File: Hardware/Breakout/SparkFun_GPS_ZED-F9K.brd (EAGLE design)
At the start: 43.2 x 43.2 mm, 104 parts, among them J1 QWIIC_RIGHT_ANGLE, J4 U.FL, J6 QWIIC_RIGHT_ANGLE, U2 3.3V, U3 UBLOX_ZED_F9K, U4 TRIPLE_BUFFER_74LVC3G07

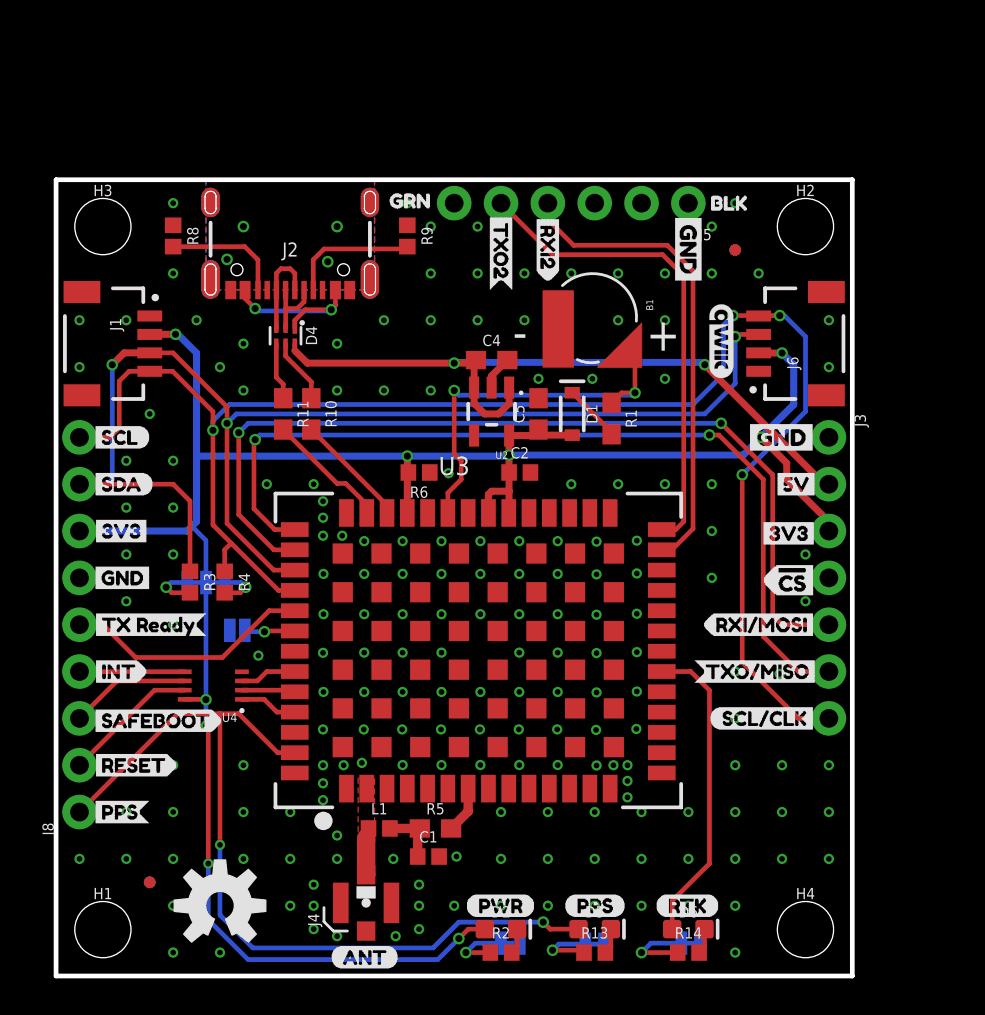
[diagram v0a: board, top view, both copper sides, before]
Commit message: Moves buzzard labels to their own folder - updates breakout board with better labeling
* fixes I2C lines being backwards
* Moves D+ and D- lines around
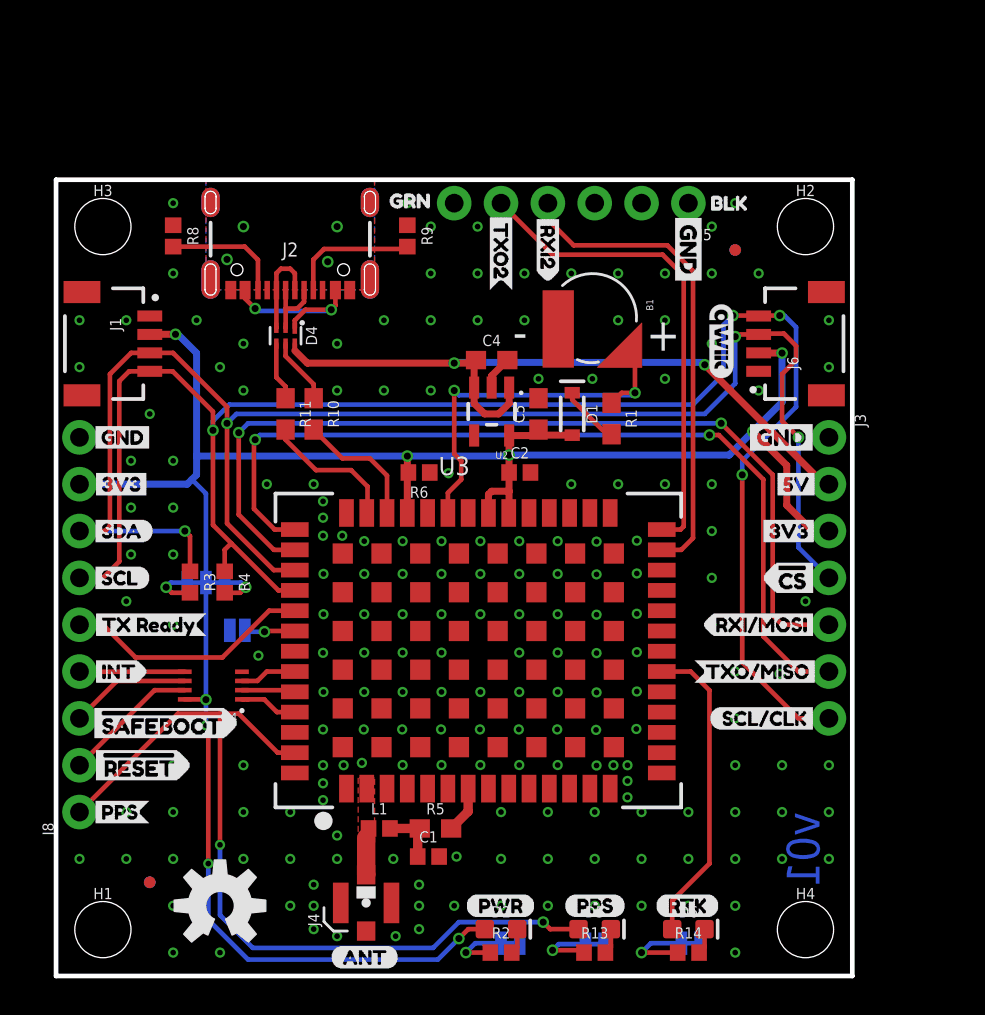
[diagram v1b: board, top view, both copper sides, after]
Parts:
- removed U$32: (no value), bottom labels:SAFEBOOT3
- added U$44: (no value), corrected_safe_reset:#RESET1
- U$10: device ALL labels:SAFEBOOT1 -> corrected_safe_reset:#SAFEBOOT0
- U$28: device bottom labels:RESET4 -> corrected_safe_reset:#SAFEBOOT3
- U$7: device ALL labels:RESET3 -> corrected_safe_reset:#RESET2
- moved U$11 7.62 mm to (1.78, 21.6)
- moved U$39 7.62 mm to (6.10, 21.6)
- moved U$41 7.62 mm to (6.48, 29.2)
- moved U$6 7.62 mm to (1.78, 29.2)
- moved U$7 5.71 mm to (7.49, 11.4), flipped to the bottom
- moved U$28 3.17 mm to (10.0, 14.0)
- moved U$40 2.54 mm to (6.35, 26.7)
- moved U$12 2.54 mm to (1.78, 24.1)
- moved U$3 2.54 mm to (1.78, 26.7)
- moved U$42 2.54 mm to (6.35, 24.1)
- moved U$10 0.40 mm to (1.40, 13.7)
- moved R10 0.13 mm to (14.0, 30.5)
- moved U$47 0.13 mm to (30.9, 3.56)
- moved R11 0.13 mm to (12.4, 30.5)
- moved U$19 0.13 mm to (38.0, 24.1)
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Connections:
- removed net !CS: J3.4
- net 3.3V: now also J8.8; no longer J8.7
- net GND: now also J8.9; no longer J8.6
- net SCL/CLK: now also J8.6; no longer J8.9
- net SDA/!CS: now also J3.4, J8.7; no longer J8.8
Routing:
- net SDA/!CS: track 69.4 -> 85.7 mm, vias 3 -> 4
- net SCL/CLK: track 86.9 -> 93.9 mm
- net DMINUS: track 6.22 -> 7.04 mm
- net DPLUS: track 6.71 -> 7.49 mm
- net GND: vias 188 -> 189
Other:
- board text added: "v01"

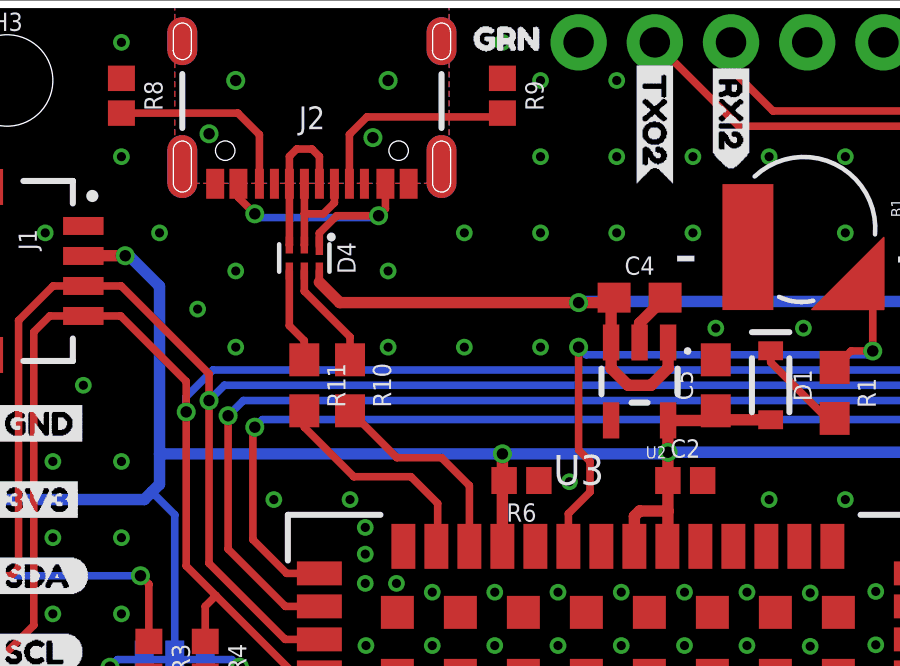
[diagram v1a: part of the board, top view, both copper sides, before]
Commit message: Fixes routing for ESD protection IC
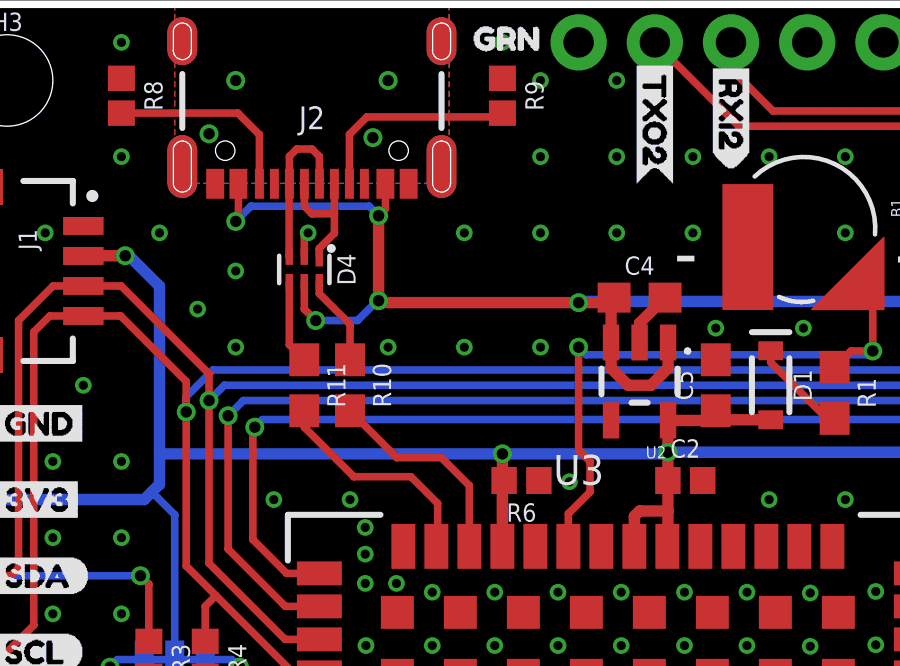
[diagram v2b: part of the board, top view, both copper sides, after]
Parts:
- moved D4 0.38 mm to (12.4, 34.3)
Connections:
- removed net N$16: D4.5, R10.1
- removed net V_USB: D4.1, J2.VBUS1, J2.VBUS2
- new net N$9: D4.6, R10.1
- net GND: now also D4.2
- net N$7: now also D4.1; no longer D4.2
- net VIN: now also D4.5, J2.VBUS1, J2.VBUS2; no longer D4.6
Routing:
- net VIN: track 39.1 -> 50.7 mm, vias 2 -> 6
- net V_USB: track 9.23 -> 0.00 mm, vias 2 -> 0
- net N$16: track 3.59 -> 0.00 mm
- net N$9: track 0.00 -> 3.00 mm
- net GND: track 1.85 -> 2.69 mm
- net N$7: track 3.83 -> 4.51 mm
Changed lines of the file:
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@@
 <attribute name="VALUE" x="26.924" y="30.48" size="0.6096" layer="27" font="vector" ratio="20" rot="R90" align="top-center"/>
 </element>
-<element name="D4" library="SparkFun-IC-Power" package="SOT886" value="PRTR5V0U2F" x="12.446" y="34.7218" smashed="yes" rot="R270">
-<attribute name="NAME" x="13.546" y="34.7218" size="0.6096" layer="25" ratio="20" rot="R270" align="bottom-center"/>
-<attribute name="PROD_ID" value="DIO-14084" x="12.446" y="34.7218" size="1.778" layer="27" font="vector" ratio="15" rot="R270" display="off"/>
-<attribute name="VALUE" x="11.546" y="34.7218" size="0.6096" layer="27" ratio="20" rot="R270" align="top-center"/>
+<element name="D4" library="SparkFun-IC-Power" package="SOT886" value="PRTR5V0U2F" x="12.446" y="34.3408" smashed="yes" rot="R270">
+<attribute name="NAME" x="13.546" y="34.3408" size="0.6096" layer="25" ratio="20" rot="R270" align="bottom-center"/>
+<attribute name="PROD_ID" value="DIO-14084" x="12.446" y="34.3408" size="1.778" layer="27" font="vector" ratio="15" rot="R270" display="off"/>
+<attribute name="VALUE" x="11.546" y="34.3408" size="0.6096" layer="27" ratio="20" rot="R270" align="top-center"/>
 </element>
 <element name="R10" library="SparkFun-Resistors" package="0603" value="27" x="13.97" y="30.48" smashed="yes" rot="R270">
@@
 <via x="17.78" y="31.75" extent="1-16" drill="0.3048"/>
 <via x="15.24" y="31.75" extent="1-16" drill="0.3048"/>
-<via x="15.24" y="34.29" extent="1-16" drill="0.3048"/>
 <via x="14.478" y="10.45" extent="1-16" drill="0.3048"/>
 <via x="14.478" y="9.5356" extent="1-16" drill="0.3048"/>
@@
 <via x="38.1" y="31.75" extent="1-16" drill="0.3048"/>
 <via x="35.56" y="34.29" extent="1-16" drill="0.3048"/>
+<contactref element="D4" pad="2"/>
+<via x="12.573" y="35.56" extent="1-16" drill="0.3048"/>
+<wire x1="12.446" y1="34.7708" x2="12.446" y2="35.433" width="0.254" layer="1"/>
+<wire x1="12.446" y1="35.433" x2="12.573" y2="35.56" width="0.254" layer="1"/>
 </signal>
 <signal name="3.3V">
@@
 <wire x1="8.114" y1="15" x2="8.128" y2="14.986" width="0.254" layer="1"/>
 <via x="8.128" y="14.986" extent="1-16" drill="0.381"/>
-<wire x1="24.572" y1="27.311" x2="24.566" y2="27.305" width="0.381" layer="1"/>
 <wire x1="24.566" y1="26.289" x2="24.566" y2="27.305" width="0.381" layer="1"/>
 <wire x1="19.048" y1="27.248" x2="19.105" y2="27.305" width="0.381" layer="1"/>
@@
 </signal>
 <signal name="VIN">
-<contactref element="D4" pad="6"/>
 <contactref element="U2" pad="1"/>
 <contactref element="U2" pad="3"/>
 <contactref element="C4" pad="1"/>
 <contactref element="J3" pad="2"/>
-<wire x1="12.946" y1="34.2918" x2="12.946" y2="33.917" width="0.254" layer="1"/>
-<wire x1="12.946" y1="33.917" x2="13.628" y2="33.235" width="0.381" layer="1"/>
 <wire x1="22.672" y1="31.9071" x2="22.672" y2="31.049" width="0.381" layer="1"/>
 <wire x1="22.672" y1="31.049" x2="23.241" y2="30.48" width="0.381" layer="1"/>
@@
 <wire x1="22.672" y1="33.301" x2="22.772" y2="33.401" width="0.381" layer="1"/>
 <wire x1="22.611" y1="33.235" x2="22.672" y2="33.174" width="0.381" layer="1"/>
-<wire x1="13.628" y1="33.235" x2="21.59" y2="33.235" width="0.381" layer="1"/>
+<wire x1="14.986" y1="33.235" x2="21.59" y2="33.235" width="0.381" layer="1"/>
 <wire x1="21.59" y1="33.235" x2="22.611" y2="33.235" width="0.381" layer="1"/>
 <wire x1="41.91" y1="26.67" x2="41.656" y2="26.67" width="0.381" layer="1"/>
@@
 <wire x1="21.59" y1="33.235" x2="21.629" y2="33.274" width="0.381" layer="16"/>
 <via x="21.59" y="33.235" extent="1-16" drill="0.381"/>
-</signal>
-<signal name="N$16">
+<contactref element="J2" pad="VBUS2"/>
+<contactref element="J2" pad="VBUS1"/>
+<wire x1="15.15" y1="36.359" x2="15.15" y2="37.1954" width="0.254" layer="1"/>
+<wire x1="14.9225" y1="36.1315" x2="15.15" y2="36.359" width="0.254" layer="1"/>
+<wire x1="10.25" y1="37.1954" x2="10.25" y2="36.031" width="0.254" layer="1"/>
+<wire x1="10.25" y1="36.031" x2="10.16" y2="35.941" width="0.254" layer="1"/>
+<via x="10.16" y="35.941" extent="1-16" drill="0.381"/>
+<wire x1="14.9225" y1="36.1315" x2="14.605" y2="36.449" width="0.254" layer="16"/>
+<wire x1="10.16" y1="35.941" x2="10.668" y2="36.449" width="0.254" layer="16"/>
+<wire x1="14.605" y1="36.449" x2="10.668" y2="36.449" width="0.254" layer="16"/>
+<via x="14.9225" y="36.1315" extent="1-16" drill="0.381"/>
 <contactref element="D4" pad="5"/>
-<contactref element="R10" pad="1"/>
-<wire x1="12.446" y1="34.2918" x2="12.446" y2="33.616" width="0.254" layer="1"/>
-<wire x1="12.446" y1="33.616" x2="13.97" y2="32.092" width="0.254" layer="1"/>
-<wire x1="13.97" y1="32.092" x2="13.97" y2="31.33" width="0.254" layer="1"/>
-</signal>
-<signal name="N$17">
-<contactref element="D4" pad="4"/>
-<contactref element="R11" pad="1"/>
-<wire x1="11.946" y1="34.2918" x2="11.946" y2="32.465" width="0.254" layer="1"/>
-<wire x1="12.446" y1="31.965" x2="11.946" y2="32.465" width="0.254" layer="1"/>
-<wire x1="12.446" y1="31.965" x2="12.446" y2="31.33" width="0.254" layer="1"/>
+<wire x1="14.9225" y1="36.1315" x2="14.9225" y2="33.2985" width="0.381" layer="1"/>
+<wire x1="14.9225" y1="33.2985" x2="14.986" y2="33.235" width="0.381" layer="1"/>
+<wire x1="12.446" y1="33.9108" x2="12.446" y2="33.02" width="0.254" layer="1"/>
+<wire x1="12.446" y1="33.02" x2="12.827" y2="32.639" width="0.254" layer="1"/>
+<via x="12.827" y="32.639" extent="1-16" drill="0.381"/>
+<wire x1="12.827" y1="32.639" x2="14.224" y2="32.639" width="0.254" layer="16"/>
+<wire x1="14.8835" y1="33.2985" x2="14.9225" y2="33.2985" width="0.254" layer="16"/>
+<via x="14.9225" y="33.2985" extent="1-16" drill="0.381"/>
+<wire x1="14.224" y1="32.639" x2="14.8835" y2="33.2985" width="0.254" layer="16"/>
 </signal>
 <signal name="N$22">
@@
 <wire x1="26.67" y1="41.021" x2="28.067" y2="39.624" width="0.254" layer="1"/>
 </signal>
-<signal name="V_USB">
-<contactref element="J2" pad="VBUS2"/>
-<contactref element="J2" pad="VBUS1"/>
-<contactref element="D4" pad="1"/>
-<wire x1="15.15" y1="36.359" x2="15.15" y2="37.1954" width="0.254" layer="1"/>
-<wire x1="12.946" y1="35.1268" x2="12.946" y2="35.552" width="0.254" layer="1"/>
-<wire x1="13.5255" y1="36.1315" x2="12.946" y2="35.552" width="0.254" layer="1"/>
-<wire x1="13.5255" y1="36.1315" x2="14.9225" y2="36.1315" width="0.254" layer="1"/>
-<wire x1="14.9225" y1="36.1315" x2="15.15" y2="36.359" width="0.254" layer="1"/>
-<wire x1="10.25" y1="37.1954" x2="10.25" y2="36.74" width="0.254" layer="1"/>
-<wire x1="10.25" y1="36.74" x2="10.795" y2="36.195" width="0.254" layer="1"/>
-<via x="10.795" y="36.195" extent="1-16" drill="0.381"/>
-<wire x1="14.859" y1="36.068" x2="10.922" y2="36.068" width="0.254" layer="16"/>
-<wire x1="10.795" y1="36.195" x2="10.922" y2="36.068" width="0.254" layer="16"/>
-<wire x1="14.9225" y1="36.1315" x2="14.859" y2="36.068" width="0.254" layer="16"/>
-<via x="14.9225" y="36.1315" extent="1-16" drill="0.381"/>
-</signal>
 <signal name="N$5">
 <contactref element="C1" pad="1"/>
@@
 <contactref element="J2" pad="B6"/>
 <contactref element="J2" pad="A6"/>
-<contactref element="D4" pad="3"/>
-<wire x1="11.95" y1="37.1954" x2="11.95" y2="35.1558" width="0.254" layer="1"/>
-<wire x1="11.95" y1="35.1558" x2="11.946" y2="35.1518" width="0.254" layer="1"/>
 <wire x1="11.95" y1="37.1954" x2="11.95" y2="38.112" width="0.254" layer="1"/>
 <wire x1="11.95" y1="38.112" x2="12.192" y2="38.354" width="0.254" layer="1"/>
@@
 <wire x1="12.7" y1="38.354" x2="12.95" y2="38.104" width="0.254" layer="1"/>
 <wire x1="12.95" y1="38.104" x2="12.95" y2="37.1954" width="0.254" layer="1"/>
+<contactref element="D4" pad="3"/>
+<wire x1="11.946" y1="34.7708" x2="11.938" y2="34.7788" width="0.254" layer="1"/>
+<wire x1="11.938" y1="37.1834" x2="11.95" y2="37.1954" width="0.254" layer="1"/>
+<wire x1="11.938" y1="34.7788" x2="11.938" y2="37.1834" width="0.254" layer="1"/>
 </signal>
 <signal name="N$7">
-<contactref element="D4" pad="2"/>
 <contactref element="J2" pad="A7"/>
 <contactref element="J2" pad="B7"/>
-<wire x1="12.45" y1="37.1954" x2="12.45" y2="36.195" width="0.254" layer="1"/>
-<wire x1="12.45" y1="36.195" x2="12.45" y2="35.1558" width="0.254" layer="1"/>
-<wire x1="12.45" y1="35.1558" x2="12.446" y2="35.1518" width="0.254" layer="1"/>
-<wire x1="13.45" y1="37.1954" x2="13.45" y2="36.564" width="0.254" layer="1"/>
-<wire x1="13.081" y1="36.195" x2="12.45" y2="36.195" width="0.254" layer="1"/>
-<wire x1="13.45" y1="36.564" x2="13.081" y2="36.195" width="0.254" layer="1"/>
+<contactref element="D4" pad="1"/>
+<wire x1="13.45" y1="36.195" x2="13.45" y2="37.1954" width="0.254" layer="1"/>
+<wire x1="12.45" y1="37.1954" x2="12.45" y2="36.445" width="0.254" layer="1"/>
+<wire x1="12.7" y1="36.195" x2="13.45" y2="36.195" width="0.254" layer="1"/>
+<wire x1="12.45" y1="36.445" x2="12.7" y2="36.195" width="0.254" layer="1"/>
+<wire x1="12.946" y1="34.7458" x2="12.946" y2="35.044" width="0.254" layer="1"/>
+<wire x1="12.946" y1="35.044" x2="13.45" y2="35.548" width="0.254" layer="1"/>
+<wire x1="13.45" y1="35.548" x2="13.45" y2="36.195" width="0.254" layer="1"/>
 </signal>
 <signal name="SHIELD">
@@
 <contactref element="J2" pad="SHLD6"/>
 </signal>
+<signal name="N$9">
+<contactref element="D4" pad="6"/>
+<contactref element="R10" pad="1"/>
+<wire x1="12.946" y1="33.9108" x2="12.946" y2="33.536" width="0.254" layer="1"/>
+<wire x1="13.97" y1="32.512" x2="13.97" y2="31.33" width="0.254" layer="1"/>
+<wire x1="12.946" y1="33.536" x2="13.97" y2="32.512" width="0.254" layer="1"/>
+</signal>
+<signal name="N$10">
+<contactref element="D4" pad="4"/>
+<contactref element="R11" pad="1"/>
+<wire x1="11.946" y1="33.9108" x2="11.946" y2="31.83" width="0.254" layer="1"/>
+<wire x1="11.946" y1="31.83" x2="12.446" y2="31.33" width="0.254" layer="1"/>
+</signal>
 </signals>
